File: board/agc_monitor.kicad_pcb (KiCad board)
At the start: 4 copper layers, 149.9 x 74.3 mm, 60 parts, among them J1 Conn_01x03, J2 Conn_01x03, J3 Conn_01x10, J4 Styx_P4, J5 Styx_P5, P1 test_connector, Q1 MMBT3904, Q2 MMBT3904, Q3 MMBT3904, Q4 MMBT3904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

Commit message: Board: more layout work
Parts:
- J1: footprint Connector_PinHeader_2.54mm:PinHeader_1x03_P2.54mm_Vertical -> Connector_PinHeader_2.00mm:PinHeader_1x03_P2.00mm_Vertical; moved to F.Cu
- R13, R14, RN10, RN12, RN14, RN9, TP2, U2: moved to B.Cu
- RN2, RN4, RN5, RN6: moved to F.Cu
- moved C2 62.8 mm to (168.5, 125.1), turned to 270 degrees
- moved L1 61.7 mm to (175.9, 124.0), turned to 90 degrees
- moved C1 61.4 mm to (171.4, 124.3), turned to 270 degrees
- moved R1 57.9 mm to (165.6, 127.8), turned to 0 degrees
- moved RN12 52.1 mm to (141.0, 114.3), turned to 90 degrees
- moved U1 49.1 mm to (163.7, 124.1)
- moved R13 45.3 mm to (159.5, 125.5), turned to 270 degrees
- moved RN16 45.1 mm to (141.0, 88.9)
- moved TP1 42.3 mm to (160.9, 128.3)
- moved RN2 40.7 mm to (113.0, 114.3)
- moved TP2 40.0 mm to (156.5, 122.2), turned to 270 degrees
- moved U2 39.8 mm to (154.9, 125.3), turned to 270 degrees
- moved RN4 39.7 mm to (141.0, 114.3)
- moved R8 39.4 mm to (115.9, 96.6), turned to 0 degrees
- moved R14 38.8 mm to (157.7, 125.5), turned to 90 degrees
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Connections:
- RN1 pad 1: MDT01 -> MSTPIT_n
- RN1 pad 2: MDT02 -> MSBSTP
- RN1 pad 3: MDT03 -> MWL09
- RN1 pad 4: MDT04 -> MWL08
- RN1 pad 5: MDT05 -> MSTP
- RN1 pad 6: MDT06 -> MSP908
- RN1 pad 7: MDT07 -> MPAL_n
- RN10 pad 1: MGOJAM -> MT06
- RN10 pad 2: MINHL -> MRCH
- RN10 pad 3: MINKL -> MAMU
- RN10 pad 4: MWLG -> MSP806
- RN10 pad 5: MONWT -> MWZG
- RN10 pad 6: MRSC -> MWYG
- RN10 pad 7: MRLG -> MSP807
- RN10 pad 8: MRGG -> MONPAR
- RN11 pad 1: MNHSBF -> MT03
- RN11 pad 2: MNHNC -> MT04
- RN11 pad 3: MNHRPT -> MSP904
- RN11 pad 4: MTCSAI -> MTCSA_n
- RN11 pad 5: MSTRT -> MWSG
- RN11 pad 6: MSTP -> MSP805
- RN11 pad 7: MSBSTP -> MWCH
- RN11 pad 8: MRDCH -> MT05
- RN12 pad 1: MGP_n -> MST1
- RN12 pad 2: MSP -> MBR1
- RN12 pad 3: MWAG -> MT01
- RN12 pad 4: MRAG -> MT02
- RN12 pad 5: MWCH -> MSP902
- RN12 pad 6: MRCH -> MST2
- RN12 pad 7: MWG -> MST3
- RN12 pad 8: MNISQ -> MSP803
- RN13 pad 1: MLDCH -> MWG
- RN13 pad 2: MONPAR -> MT09
- RN13 pad 3: MONWBK -> MT10
- RN13 pad 4: MLOAD -> MNISQ
- RN13 pad 5: MREAD -> DOSCAL
- RN13 pad 6: MAMU -> MSQ10
- RN13 pad 7: DOSCAL -> MSQ11
- RN14 pad 2: MWATCH_n -> MT11
- RN14 pad 3: MON800 -> MT12
- RN14 pad 4: MPIPAL_n -> MWATCH_n
- RN14 pad 5: MSCDBL_n -> MSP912
- RN14 pad 7: OUTCOM -> MSQ12
- RN14 pad 8: MSCAFL_n -> MSQ13
- RN15 pad 1: MOSCAL_n -> OUTCOM
- RN15 pad 2: MVFAIL_n -> MLOAD
- RN15 pad 3: SIGNY_n -> MRULOG
- RN15 pad 4: MSP803 -> MWFBG
- RN15 pad 5: MSP805 -> MREAD
- RN15 pad 6: MSP806 -> MSCAFL_n
- RN15 pad 7: MSP807 -> MSQ14
- RN15 pad 8: MSP902 -> MSQEXT
- RN16 pad 1: MSP904 -> MOSCAL_n
- RN16 pad 2: MSP908 -> MON800
- RN16 pad 3: MSP910 -> MWEBG
- RN16 pad 4: MSP912 -> MWBBEG
- RN16 pad 5: MSP914 -> MPIPAL_n
- RN16 pad 7: NHALGA -> MVFAIL_n
- RN16 pad 8: Net-(RN16-Pad8) -> MSQ16
- RN2 pad 1: MWL01 -> MDT07
- RN2 pad 2: MWL02 -> MSTRT
- RN2 pad 3: MWL03 -> MWL07
- RN2 pad 4: MWL04 -> MWL06
- RN2 pad 5: MWL05 -> MTCSAI
- RN2 pad 6: MWL06 -> MRPTAL_n
- RN2 pad 7: MWL07 -> MDT06
- RN2 pad 8: MWL08 -> MDT05
- RN3 pad 1: MDT09 -> MTCAL_n
- RN3 pad 2: MDT10 -> MNHRPT
- RN3 pad 3: MDT11 -> MWL05
- RN3 pad 4: MDT12 -> MWL04
- RN3 pad 5: MDT13 -> MNHNC
- RN3 pad 6: MDT14 -> MCTRAL_n
- RN3 pad 7: MDT15 -> MDT04
- RN3 pad 8: MDT16 -> MDT03
- RN4 pad 1: MWL09 -> MIIP
- RN4 pad 2: MWL10 -> MNHSBF
- RN4 pad 3: MWL11 -> MWL03
- RN4 pad 4: MWL12 -> MWL02
- RN4 pad 5: MWL13 -> MBR2
- RN4 pad 6: MWL14 -> MDT02
- RN4 pad 7: MWL15 -> MDT01
- RN4 pad 8: MWL16 -> MWL01
- RN5 pad 1: MT01 -> SIGNY_n
- RN5 pad 2: MT02 -> MWL16
- RN5 pad 3: MT03 -> MRAG
- RN5 pad 4: MT04 -> MRLG
- RN5 pad 5: MT05 -> MDT16
- RN5 pad 6: MT06 -> MDT15
- RN5 pad 7: MT07 -> MRSC
- RN5 pad 8: MT08 -> MWAG
- RN6 pad 1: MT09 -> MWL15
- RN6 pad 2: MT10 -> MWL14
- RN6 pad 3: MT11 -> MRGG
- RN6 pad 4: MT12 -> MSP914
- RN6 pad 5: MRULOG -> MONWT
- RN6 pad 6: MWFBG -> MDT14
- RN6 pad 7: MWEBG -> MDT13
- RN6 pad 8: MWBBEG -> MWLG
- RN7 pad 1: MST1 -> MSP
- RN7 pad 2: MST2 -> MWL13
- RN7 pad 3: MST3 -> MWL12
- RN7 pad 4: MTCSA_n -> MGP_n
- RN7 pad 5: MWSG -> MINKL
- RN7 pad 6: MWZG -> MDT12
- RN7 pad 7: MWYG -> MDT11
- RN7 pad 8: MWQG -> MINHL
- RN8 pad 1: MWBG -> MLDCH
- RN8 pad 2: MSQ10 -> MWL11
- RN8 pad 3: MSQ11 -> MWL10
- RN8 pad 4: MSQ12 -> MRDCH
- RN8 pad 5: MSQ13 -> MSP910
- RN8 pad 6: MSQ14 -> MGOJAM
- RN8 pad 7: MSQEXT -> MDT10
- RN8 pad 8: MSQ16 -> MDT09
- RN9 pad 1: MBR1 -> MT07
- RN9 pad 2: MBR2 -> MT08
- RN9 pad 3: MIIP -> MONWBK
- RN9 pad 4: MCTRAL_n -> MSCDBL_n
- RN9 pad 5: MTCAL_n -> MWQG
- RN9 pad 6: MRPTAL_n -> MWBG
- RN9 pad 7: MPAL_n -> NHALGA
- RN9 pad 8: MSTPIT_n -> Net-(RN9-Pad8)
- U2 pad 5: +3V3_AGC -> +3V3_FPGA
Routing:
- net NHALGA: track 22.9 -> 130.0 mm
- net MWG: track 26.1 -> 112.3 mm
- net MSBSTP: track 28.8 -> 114.4 mm
- net MT09: track 38.6 -> 123.4 mm
- net MWL09: track 41.2 -> 125.4 mm
- net MWBG: track 34.9 -> 119.0 mm
- net MT10: track 38.7 -> 122.1 mm
- net MWQG: track 34.9 -> 117.6 mm
- net MWL08: track 41.2 -> 123.9 mm
- net MNISQ: track 26.4 -> 108.3 mm
- net MSTP: track 28.7 -> 110.0 mm
- net MSCDBL_n: track 22.8 -> 104.1 mm
- net DOSCAL: track 23.6 -> 104.1 mm
- net MONWBK: track 26.1 -> 106.0 mm
- net MSP908: track 18.7 -> 98.6 mm
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
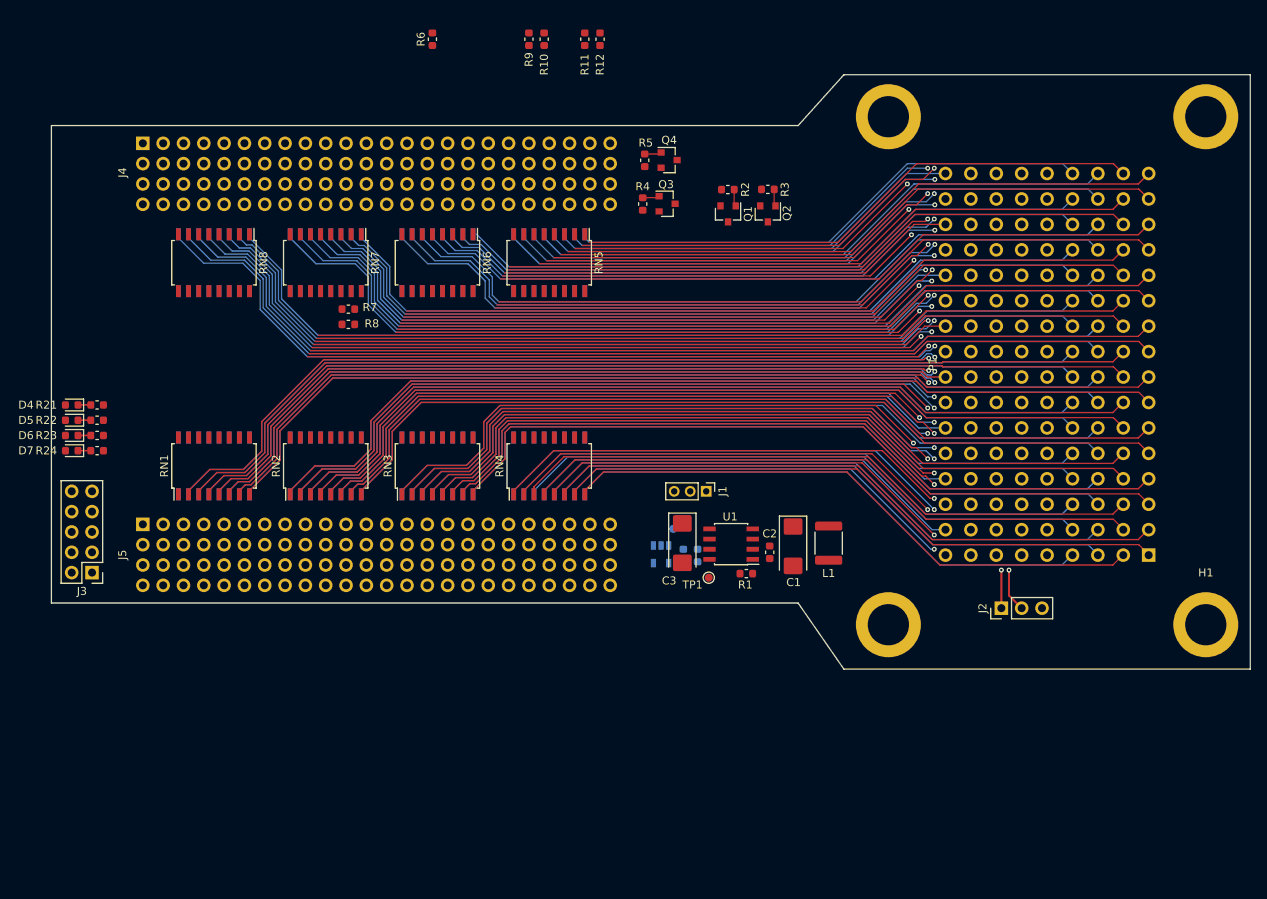
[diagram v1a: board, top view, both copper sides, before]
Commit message: Board: lots of work routing connector J4. It's almost fully wired up; J5 is next.
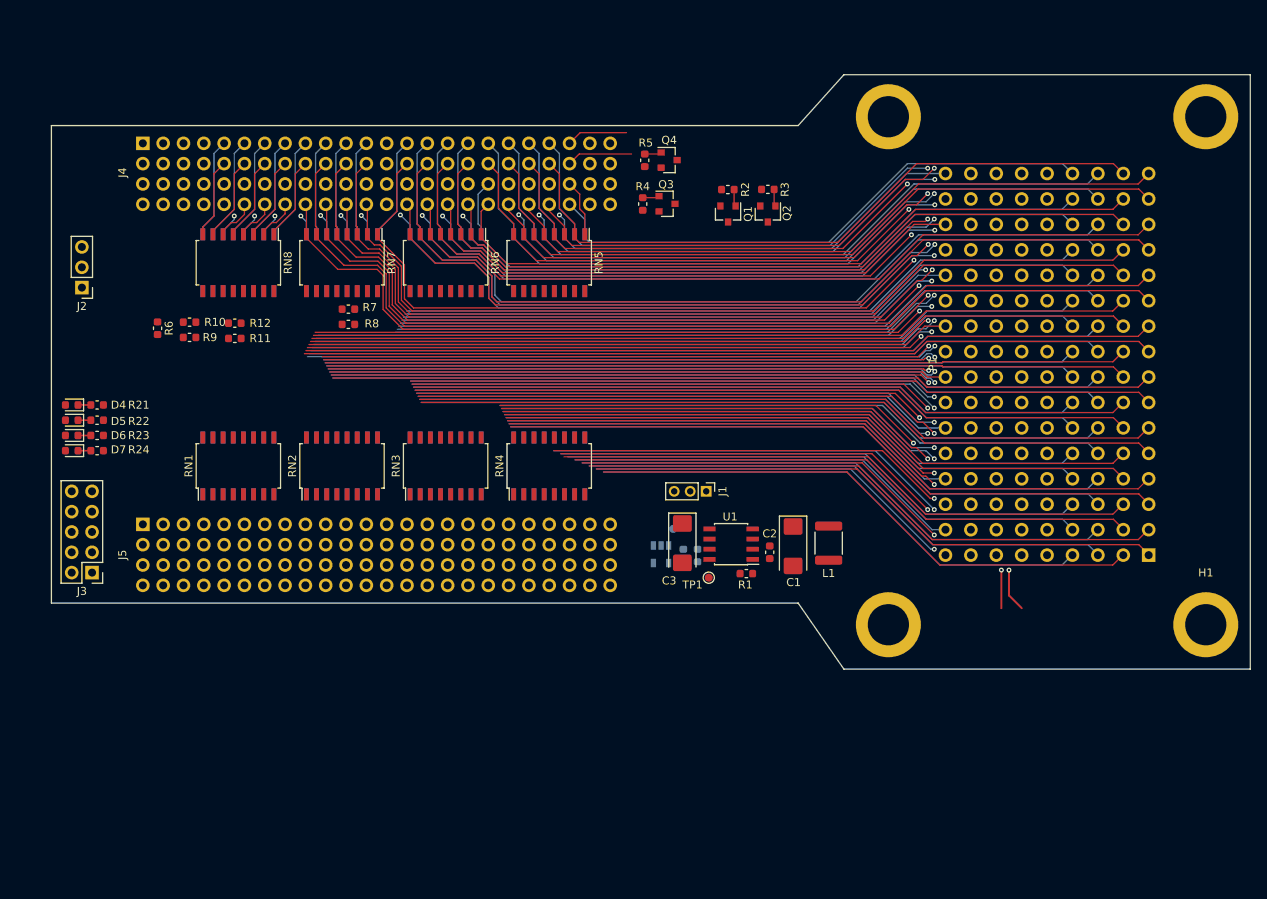
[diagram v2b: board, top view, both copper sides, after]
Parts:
- moved J2 121.7 mm to (82.5, 92.0), turned to 180 degrees
- moved R12 57.8 mm to (101.7, 96.5), turned to 180 degrees
- moved R11 57.6 mm to (101.7, 98.4), turned to 0 degrees
- moved R10 56.7 mm to (96.0, 96.3), turned to 180 degrees
- moved R9 56.5 mm to (96.0, 98.2), turned to 0 degrees
- moved R6 49.9 mm to (92.0, 97.1), turned to 270 degrees
- moved RN1 3.05 mm to (102.1, 114.3)
- moved RN13 3.05 mm to (102.1, 88.9)
- moved RN8 3.05 mm to (102.1, 88.9)
- moved RN9 3.05 mm to (102.1, 114.3)
- moved RN10 2.03 mm to (115.1, 114.3)
- moved RN14 2.03 mm to (115.1, 88.9)
- moved RN2 2.03 mm to (115.1, 114.3)
- moved RN7 2.03 mm to (115.1, 88.9)
- moved RN11 1.02 mm to (128.0, 114.3)
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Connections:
- J4 pad 1: Net-(J4-Pad1) -> GND
- J4 pad 13: MWCH -> Net-(J4-Pad13)
- J4 pad 14: MRCH -> Net-(J4-Pad14)
- J4 pad 17: MWL01 -> MWG
- J4 pad 18: MWL02 -> MDT09
- J4 pad 19: MWL03 -> Net-(J4-Pad19)
- J4 pad 20: MWL04 -> Net-(J4-Pad20)
- J4 pad 21: MWL05 -> MT09
- J4 pad 22: MWL06 -> MDT10
- J4 pad 23: MWL07 -> MT10
- J4 pad 24: MWL08 -> MGOJAM
- J4 pad 25: MWL09 -> MNISQ
- J4 pad 26: MWL10 -> MSP910
- J4 pad 27: MWL11 -> DOSCAL
- J4 pad 28: MWL12 -> MRDCH
- J4 pad 29: MWL13 -> MSQ10
- J4 pad 30: MWL14 -> MWL10
- J4 pad 31: MWL15 -> MSQ11
- J4 pad 32: MWL16 -> MWL11
- J4 pad 33: MT01 -> DBLTST
- J4 pad 34: MT02 -> MLDCH
- J4 pad 35: MT03 -> MREQIN
- J4 pad 36: MT04 -> MINHL
- J4 pad 37: MT05 -> MT11
- J4 pad 38: MT06 -> MDT11
- J4 pad 39: MT07 -> MT12
- J4 pad 40: MT08 -> MDT12
- J4 pad 41: MT09 -> MWATCH_n
- J4 pad 42: MT10 -> MINKL
- J4 pad 43: MT11 -> MSP912
- J4 pad 44: MT12 -> MGP_n
- J4 pad 45: Net-(J4-Pad1) -> MWARNF_n
- J4 pad 46: ADC_3V3_P -> MWL12
- J4 pad 47: /StyxConnectors/DBG1 -> MSQ12
- J4 pad 48: /StyxConnectors/DBG2 -> MWL13
- J4 pad 49: Net-(J4-Pad1) -> GND
- J4 pad 5: MWG -> Net-(J4-Pad5)
- J4 pad 53: MST1 -> MSQ13
- J4 pad 54: MST2 -> MSP
- J4 pad 55: MST3 -> OUTCOM
- J4 pad 56: MTCSA_n -> MWLG
- J4 pad 57: MWSG -> MLOAD
- J4 pad 58: MWZG -> MDT13
- J4 pad 59: MWYG -> MRULOG
- J4 pad 6: MNISQ -> Net-(J4-Pad6)
- J4 pad 60: MWQG -> MDT14
- J4 pad 61: MWBG -> MWFBG
- J4 pad 62: MSQ10 -> MONWT
- J4 pad 63: MSQ11 -> MREAD
- J4 pad 64: MSQ12 -> MSP914
- J4 pad 65: MSQ13 -> MSCAFL_n
- J4 pad 66: MSQ14 -> MRGG
- J4 pad 67: MSQEXT -> MSQ14
- J4 pad 68: MSQ16 -> MWL14
- J4 pad 69: MBR1 -> MOSCAL_n
- J4 pad 7: MREQIN -> Net-(J4-Pad7)
- J4 pad 70: MBR2 -> MWAG
- J4 pad 71: MIIP -> MSQEXT
- J4 pad 72: MCTRAL_n -> MWL15
- J4 pad 73: MTCAL_n -> MWEBG
- J4 pad 74: MRPTAL_n -> MDT15
- J4 pad 75: MPAL_n -> MON800
- J4 pad 76: MSTPIT_n -> MRSC
- J4 pad 77: MGOJAM -> MPIPAL_n
- J4 pad 78: MINHL -> MRLG
- J4 pad 79: MINKL -> MWBBEG
- J4 pad 8: MWATCH_n -> Net-(J4-Pad8)
- J4 pad 80: MWLG -> MDT16
- J4 pad 81: MONWT -> MVFAIL_n
- J4 pad 82: MRSC -> MWL16
- J4 pad 83: MRLG -> MSP916
- J4 pad 84: MGP_n -> MRAG
- J4 pad 85: MSP -> NHSTRT1
- J4 pad 86: MRGG -> NHSTRT2
- J4 pad 87: MWAG -> SIGNY_n
- J4 pad 88: MRAG -> MSQ16
- J4 pad 9: Net-(J4-Pad1) -> GND
- J5 pad 12: MWARNF_n -> Net-(J5-Pad12)
- J5 pad 15: OUTCOM -> Net-(J5-Pad15)
- J5 pad 16: MSCAFL_n -> Net-(J5-Pad16)
- J5 pad 17: MOSCAL_n -> Net-(J5-Pad17)
- J5 pad 18: MVFAIL_n -> Net-(J5-Pad18)
- J5 pad 19: SIGNY_n -> Net-(J5-Pad19)
- J5 pad 20: NHSTRT2 -> Net-(J5-Pad20)
- J5 pad 29: MDT09 -> Net-(J5-Pad29)
- J5 pad 30: MDT10 -> Net-(J5-Pad30)
- J5 pad 31: MDT11 -> Net-(J5-Pad31)
- J5 pad 32: MDT12 -> Net-(J5-Pad32)
- J5 pad 33: MDT13 -> Net-(J5-Pad33)
- J5 pad 34: MDT14 -> Net-(J5-Pad34)
- J5 pad 35: MDT15 -> Net-(J5-Pad35)
- J5 pad 36: MDT16 -> Net-(J5-Pad36)
- J5 pad 43: MLDCH -> Net-(J5-Pad43)
- J5 pad 44: MRDCH -> Net-(J5-Pad44)
- J5 pad 55: MLOAD -> Net-(J5-Pad55)
- J5 pad 56: MREAD -> Net-(J5-Pad56)
- J5 pad 57: DOSCAL -> Net-(J5-Pad57)
- J5 pad 58: DBLTST -> Net-(J5-Pad58)
- J5 pad 61: MRULOG -> Net-(J5-Pad61)
- J5 pad 62: MWFBG -> Net-(J5-Pad62)
- J5 pad 63: MWEBG -> Net-(J5-Pad63)
- J5 pad 64: MWBBEG -> Net-(J5-Pad64)
- J5 pad 7: MON800 -> Net-(J5-Pad7)
- J5 pad 73: MSP910 -> Net-(J5-Pad73)
- J5 pad 74: MSP912 -> Net-(J5-Pad74)
- J5 pad 75: MSP914 -> Net-(J5-Pad75)
- J5 pad 76: MSP916 -> Net-(J5-Pad76)
- J5 pad 8: MPIPAL_n -> Net-(J5-Pad8)
- J5 pad 86: NHSTRT1 -> Net-(J5-Pad86)
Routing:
- net MSP: track 68.9 -> 100.5 mm
- net MDT11: track 96.1 -> 123.3 mm
- net MSBSTP: track 114.4 -> 88.1 mm
- net NHALGA: track 130.0 -> 103.7 mm
- net MWBG: track 119.0 -> 94.0 mm
- net MWL09: track 125.4 -> 100.4 mm
- net MINKL: track 83.0 -> 107.7 mm
- net MDT13: track 84.9 -> 109.6 mm
- net MWQG: track 117.6 -> 93.8 mm
- net MWL08: track 123.9 -> 100.1 mm
- net MONPAR: track 98.0 -> 74.8 mm
- net MDT07: track 116.6 -> 93.4 mm
- net MINHL: track 83.7 -> 106.6 mm
- net MSTP: track 110.0 -> 87.5 mm
- net MSCDBL_n: track 104.1 -> 81.6 mm
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
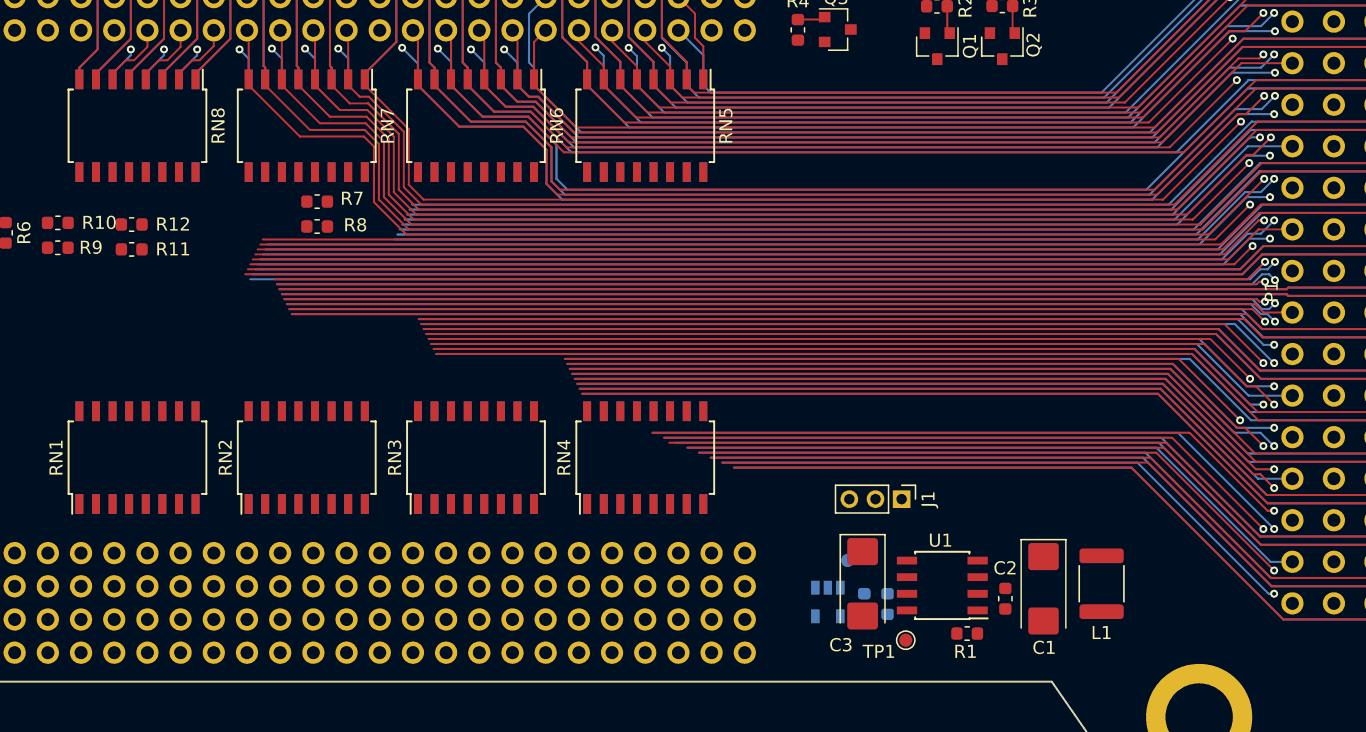
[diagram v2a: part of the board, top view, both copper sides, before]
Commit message: Board: completed routing of AGC signals to RNs and FPGA pins
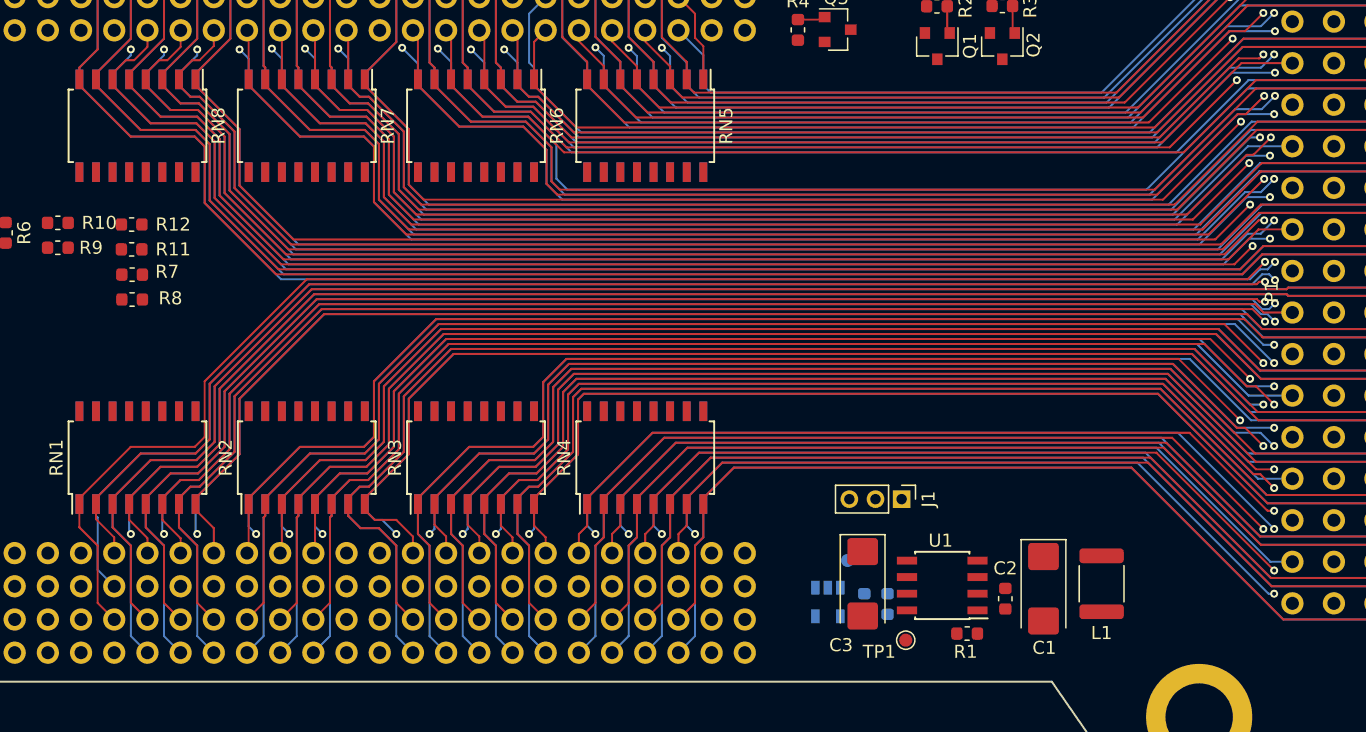
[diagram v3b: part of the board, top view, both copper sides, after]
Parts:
- moved R8 15.2 mm to (101.7, 102.2)
- moved R7 15.2 mm to (101.7, 100.3)
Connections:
- J5 pad 11: MSCDBL_n -> Net-(J5-Pad11)
- J5 pad 17: Net-(J5-Pad17) -> MSBSTP
- J5 pad 18: Net-(J5-Pad18) -> NHALGA
- J5 pad 19: Net-(J5-Pad19) -> MSTPIT_n
- J5 pad 21: MDT01 -> MWL08
- J5 pad 22: MDT02 -> MWQG
- J5 pad 23: MDT03 -> MWL09
- J5 pad 24: MDT04 -> MWBG
- J5 pad 25: MDT05 -> MSP908
- J5 pad 26: MDT06 -> MONWBK
- J5 pad 27: MDT07 -> MSTP
- J5 pad 28: MDT08 -> MSCDBL_n
- J5 pad 29: Net-(J5-Pad29) -> MDT08
- J5 pad 30: Net-(J5-Pad30) -> MT07
- J5 pad 31: Net-(J5-Pad31) -> MPAL_n
- J5 pad 32: Net-(J5-Pad32) -> MT08
- J5 pad 33: Net-(J5-Pad33) -> MDT07
- J5 pad 34: Net-(J5-Pad34) -> MONPAR
- J5 pad 35: Net-(J5-Pad35) -> MSTRT
- J5 pad 36: Net-(J5-Pad36) -> MSP807
- J5 pad 37: MNHSBF -> MWL07
- J5 pad 38: MNHNC -> MWYG
- J5 pad 39: MNHRPT -> MWL06
- J5 pad 40: MTCSAI -> MWZG
- J5 pad 41: MSTRT -> MTCSAI
- J5 pad 42: MSTP -> MSP806
- J5 pad 43: Net-(J5-Pad43) -> MRPTAL_n
- J5 pad 44: Net-(J5-Pad44) -> MAMU
- J5 pad 53: MONPAR -> MDT05
- J5 pad 54: MONWBK -> MT06
- J5 pad 55: Net-(J5-Pad55) -> MDT06
- J5 pad 56: Net-(J5-Pad56) -> MRCH
- J5 pad 57: Net-(J5-Pad57) -> MNHRPT
- J5 pad 58: Net-(J5-Pad58) -> MWCH
- J5 pad 59: MAMU -> MTCAL_n
- J5 pad 60: MSBSTP -> MT05
- J5 pad 61: Net-(J5-Pad61) -> MWL04
- J5 pad 62: Net-(J5-Pad62) -> MWSG
- J5 pad 63: Net-(J5-Pad63) -> MWL05
- J5 pad 64: Net-(J5-Pad64) -> MSP805
- J5 pad 65: EN_3V3_AGC -> MCTRAL_n
- J5 pad 66: MSP803 -> MSP904
- J5 pad 67: MSP805 -> MNHNC
- J5 pad 68: MSP806 -> MTCSA_n
- J5 pad 69: MSP807 -> MDT03
- J5 pad 70: MSP902 -> MT03
- J5 pad 71: MSP904 -> MDT04
- J5 pad 72: MSP908 -> MT04
- J5 pad 73: Net-(J5-Pad73) -> MIIP
- J5 pad 74: Net-(J5-Pad74) -> MSP803
- J5 pad 75: Net-(J5-Pad75) -> MNHSBF
- J5 pad 76: Net-(J5-Pad76) -> MST3
- J5 pad 77: /StyxConnectors/LED1 -> MWL03
- J5 pad 78: /StyxConnectors/LED2 -> MST2
- J5 pad 79: /StyxConnectors/LED3 -> MWL02
- J5 pad 80: /StyxConnectors/LED4 -> MSP902
- J5 pad 81: /StyxConnectors/DBG3 -> MBR2
- J5 pad 82: /StyxConnectors/DBG4 -> MT02
- J5 pad 83: /StyxConnectors/DBG5 -> MDT02
- J5 pad 84: /StyxConnectors/DBG6 -> MT01
- J5 pad 85: NHALGA -> MDT01
- J5 pad 86: Net-(J5-Pad86) -> MBR1
- J5 pad 87: /StyxConnectors/DBG7 -> MWL01
- J5 pad 88: /StyxConnectors/DBG8 -> MST1
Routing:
- net MWBG: track 94.0 -> 128.8 mm
- net MSTPIT_n: track 91.9 -> 126.7 mm
- net MSP807: track 71.9 -> 104.2 mm
- net MSCDBL_n: track 81.6 -> 113.9 mm
- net MWL09: track 100.4 -> 132.6 mm
- net MT05: track 77.2 -> 108.0 mm
- net NHALGA: track 103.7 -> 134.1 mm
- net MWZG: track 84.1 -> 114.0 mm
- net MT08: track 97.0 -> 126.9 mm
- net MSTRT: track 78.2 -> 108.0 mm
- net MSTP: track 87.5 -> 117.2 mm
- net MONPAR: track 74.8 -> 103.7 mm, vias 1 -> 2
- net MRCH: track 74.6 -> 103.1 mm
- net MSP805: track 61.7 -> 90.1 mm
- net MTCAL_n: track 70.8 -> 99.1 mm
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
